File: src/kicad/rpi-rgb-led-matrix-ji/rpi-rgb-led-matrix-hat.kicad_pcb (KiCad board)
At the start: 2 copper layers, 65 x 56 mm, 39 parts, among them J3 Screw_Terminal_01x02, J4 Conn_02x08_Odd_Even, J5 Conn_02x08_Odd_Even, J6 Conn_02x08_Odd_Even, P1 Raspberry_Pi_2_3, Q1 DMG2305UX, Q2 DMMT5401, U1 74HCT245, U2 74HCT245, U3 74HCT245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

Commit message: fixed g1/g2 inversion, removed virtual diode bypass
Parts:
- removed SP1, SP2: SP, jicad:smd1mm4pad1
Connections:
- P1 pad 10: /G2_1 -> /G1_1
- P1 pad 11: /G1_1 -> /G2_1
- P1 pad 21: /G1_2 -> /G2_2
- P1 pad 22: /G2_2 -> /G1_2
- P1 pad 31: /G1_3 -> /G2_3
- P1 pad 32: /G2_3 -> /G1_3
- U1 pad 2: /G1_1 -> /G2_1
- U1 pad 3: /G2_1 -> /G1_1
- U2 pad 2: /G1_2 -> /G2_2
- U2 pad 3: /G2_2 -> /G1_2
- U4 pad 2: /G1_3 -> /G2_3
- U4 pad 3: /G2_3 -> /G1_3
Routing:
- net /HAT_5V: track 39.1 -> 25.2 mm
- net /G2_2: track 9.95 -> 6.88 mm
- net /G1_2: track 6.88 -> 9.95 mm
- net /G2_3: track 9.35 -> 6.36 mm
- net /G1_3: track 6.36 -> 9.35 mm
- net /G2_1: track 9.95 -> 7.94 mm
- net /G1_1: track 7.94 -> 9.95 mm
- net +5V: track 124.1 -> 122.2 mm
- net GND: vias 18 -> 17
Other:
- board text added: "v1.2.3 20190324"
- board text removed: "v1.2.2 20190315"

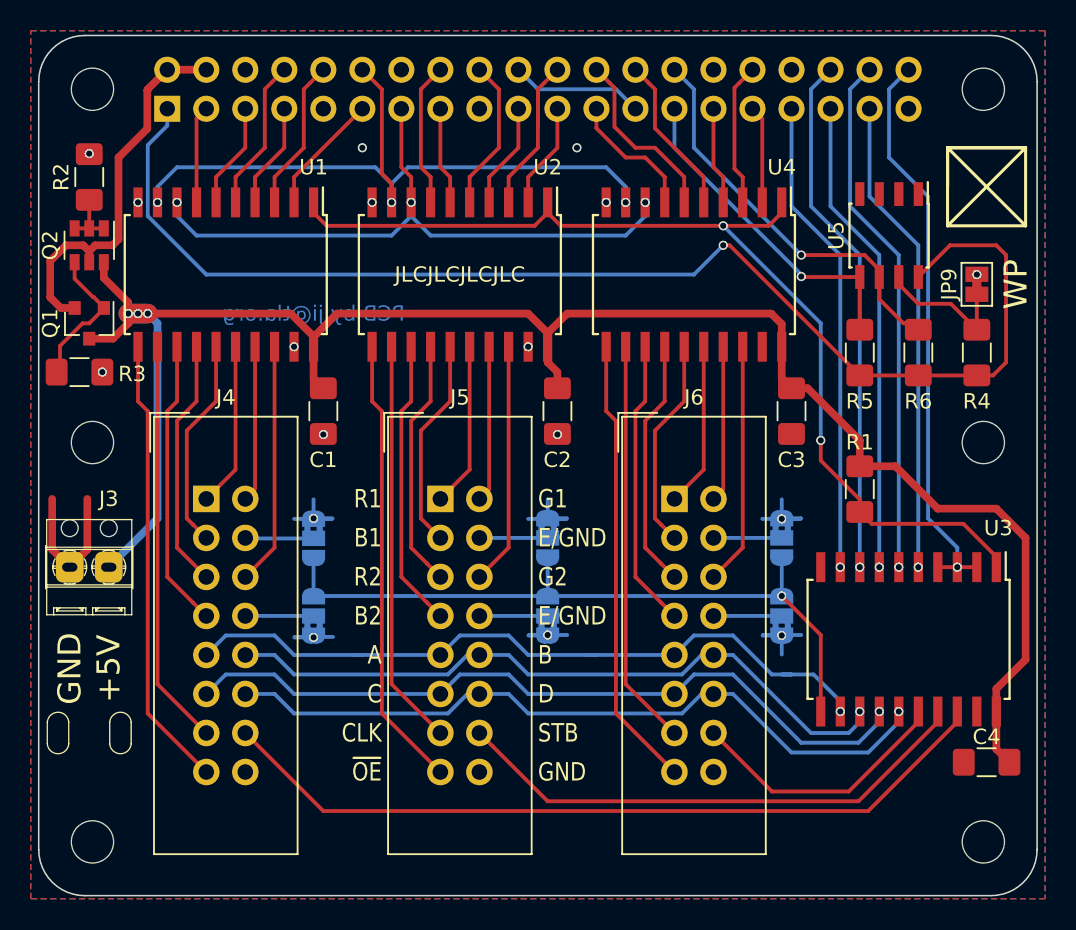
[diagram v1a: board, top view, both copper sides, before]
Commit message: cleaned up PSU circuitry; added bypass capacitor to EEPROM
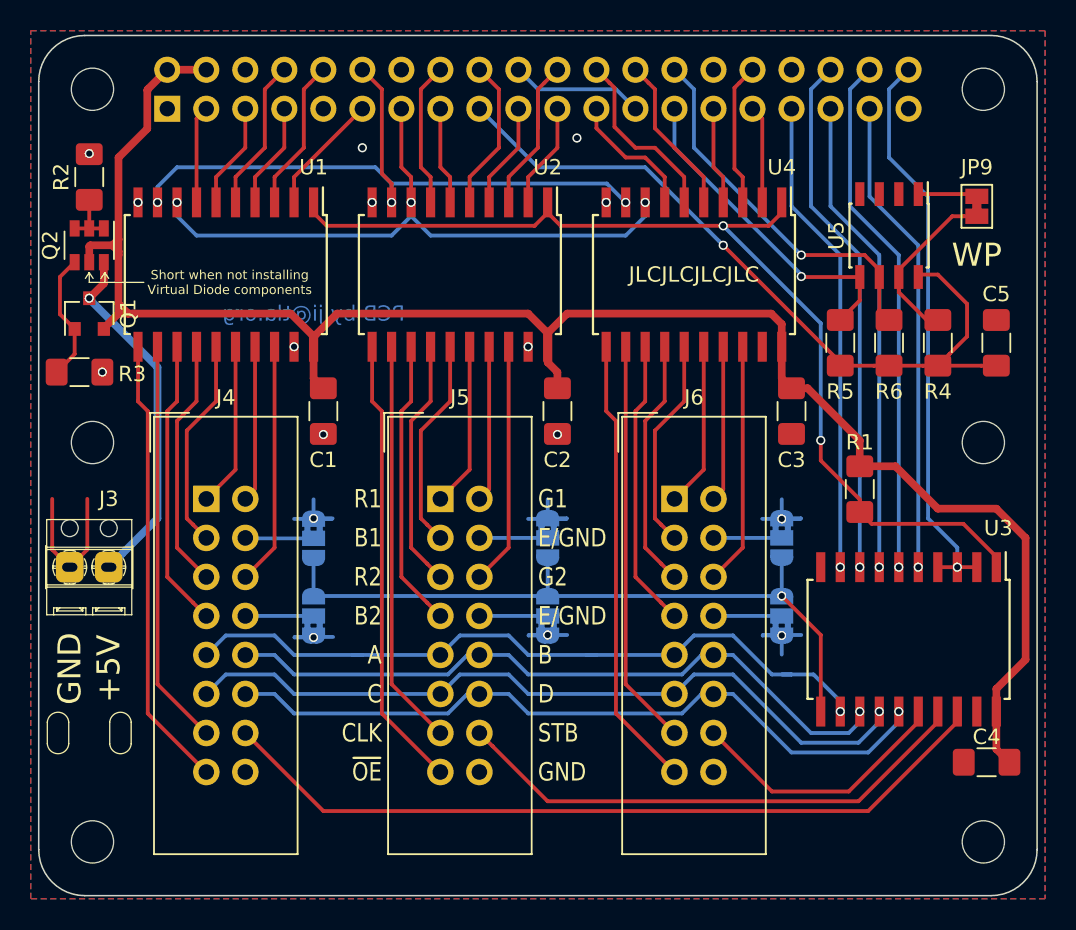
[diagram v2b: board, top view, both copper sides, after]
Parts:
- added C5: 100nF, Capacitor_SMD:C_1206_3216Metric_Pad1.42x1.75mm_HandSolder, F.Cu at (54.0, 15.2)
- moved JP9 5.08 mm to (52.7, 6.35)
- moved R4 2.62 mm to (50.2, 15.2)
- moved R6 2.01 mm to (47.0, 15.2)
- moved R5 1.42 mm to (43.8, 15.2)
- moved Q1 0.63 mm to (-5.08, 13.3), turned to 90 degrees
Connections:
- J3 pad 1: +5V -> +5VP
- P1 pad 1: +3V3 -> (no net)
- P1 pad 17: (no net) -> +3V3
- P1 pad 2: /HAT_5V -> +5V
- P1 pad 4: /HAT_5V -> +5V
- Q1 pad 2: /HAT_5V -> +5V
- Q1 pad 3: +5V -> +5VP
- Q2 pad 5: /HAT_5V -> +5V
- Q2 pad 6: +5V -> +5VP
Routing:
- net +3V3: track 83.9 -> 49.6 mm
- net /HAT_5V: track 25.2 -> 0.00 mm
- net +5VP: track 0.00 -> 23.4 mm, vias 0 -> 1
- net GND: track 48.5 -> 52.4 mm, vias 17 -> 16
- net Net-(JP9-Pad1): track 9.09 -> 11.3 mm
- net +5V: track 122.2 -> 120.3 mm, vias 3 -> 0
- net /ID_SC: track 26.2 -> 24.5 mm
- net /~OE: track 45.1 -> 43.6 mm
- net Net-(Q1-Pad1): track 9.50 -> 8.43 mm
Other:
- board text added: "Bug: bridged solder jumpers report pads too close in DRC. Ignore the complaints on the solder jumpers."
- board text added: "v1.2.4 20190327"
- board text removed: "Bug: bridged solder jumpers report pads too close in DRC. Ignore the 8 complaints on the 8 solder jumpers."
- board text removed: "Reserved space for POE connector"
- board text removed: "v1.2.3 20190324"
